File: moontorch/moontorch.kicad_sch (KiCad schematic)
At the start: 27 parts, among them J1 Conn_Coaxial, J2 Pogo_VLED_1, J3 Pogo_VLED_2, J4 BAT, J5 Torchbutton, J6 UART, J7 USB, J8 Pogo_GND, Q1 AP2317SD, SW3 RESET, SW4 BOOT, U1 HT-CT62, U2 L80-R, U3 XTX XTP2038-330AS2CT

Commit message: weiter moontorch
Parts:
- removed J1: Conn_Coaxial, Connector_Coaxial:SMA_Amphenol_132289_EdgeMount, symbol Connector:Conn_Coaxial
- added C8: 1u, Capacitor_SMD:C_0603_1608Metric_Pad1.08x0.95mm_HandSolder, symbol Device:C
- added R6: 0R, Resistor_SMD:R_0603_1608Metric_Pad0.98x0.95mm_HandSolder, symbol Device:R
- added R8, R9: 10K, Resistor_SMD:R_0603_1608Metric_Pad0.98x0.95mm_HandSolder, symbol Device:R
- added RF1: 443MHz, EasyEDA:SMA-SMD_BWSMA-KE-P001, symbol EasyEDA:HJ-SMA275
- added U4: 2.4GHz, EasyEDA:ANT-SMD_L5.0-W2.0, symbol EasyEDA:2450AT42A100E
- C1, C2, C7: LCSC Part (none) -> C15849
- C3, C4: LCSC Part (none) -> C14663
- C5, C6: LCSC Part (none) -> C19702
- J2, J3, J8: footprint TestPoint:TestPoint_Pad_3.0x3.0mm -> hacrafu:Pogo Pin 3015; LCSC Part (none) -> C5221293
- J4: footprint Connector_JST:JST_XH_B2B-XH-A_1x02_P2.50mm_Vertical -> Connector_PinHeader_2.54mm:PinHeader_1x02_P2.54mm_Horizontal
- R1, R2, R3: LCSC Part (none) -> C98220
- R4, R5: LCSC Part (none) -> C25803
- U3: LCSC Part (none) -> C7422361
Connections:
- net +3V3: now also C8.1, R8.2, R9.1
- net GND: now also C8.2, RF1.1, RF1.2, RF1.3, RF1.4
- net GPS_PPS: now also R9.2
- net USB_DN: now reaches U1.17 (GPIO18_DN)
- net USB_DN: now also J7.3 (Pin_3); no longer J7.2 (Pin_2)
- net USB_DP: now reaches U1.18 (GPIO19_DP)
- net USB_DP: now also J7.2 (Pin_2); no longer J7.3 (Pin_3)
- net at U1.22 (LoRa_Ant): now also RF1.5
- net UART_TX: now reaches J6.2 (Pin_2), U1.20 (GPIO21_TXD)
- net UART_RX: now reaches J6.3 (Pin_3), U1.19 (GPIO20_RXD)
- net at U1.1 (2.4G_Ant): now also R6.2
- net at U1.16 (GPIO8): now also R8.1
- new net: R6.1, U4.1 (ANT)
- no-connect marks 4 -> 6
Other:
- moved on the sheet: C7, J5, J7

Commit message: zwischenstand bestellfähig 1
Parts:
- removed BT1: Battery, hacrafu:Battery 230525, symbol Device:Battery
- removed J2: Pogo_VLED_1, hacrafu:Pogo Pin 3015, symbol Connector:Conn_01x01_Pin
- removed J3: Pogo_VLED_2, hacrafu:Pogo Pin 3015, symbol Connector:Conn_01x01_Pin
- removed J5: Torchbutton, hacrafu:Tochbutton GND, symbol Connector:Conn_01x01_Pin
- removed J7: USB, Connector_PinHeader_2.54mm:PinHeader_1x03_P2.54mm_Vertical, symbol Connector:Conn_01x03_Pin
- removed J8: Pogo_GND, hacrafu:Pogo Pin 3015, symbol Connector:Conn_01x01_Pin
- removed R6: 0R, Resistor_SMD:R_0603_1608Metric_Pad0.98x0.95mm_HandSolder, symbol Device:R
- removed RF1: 443MHz, EasyEDA:SMA-SMD_BWSMA-KE-P001, symbol EasyEDA:HJ-SMA275
- removed U4: 2.4GHz, EasyEDA:ANT-SMD_L5.0-W2.0, symbol EasyEDA:2450AT42A100E
- added C10, C12, C13, C9: 1u, Capacitor_SMD:C_0603_1608Metric_Pad1.08x0.95mm_HandSolder, symbol Device:C
- added C4, C7: 10u, Capacitor_SMD:C_0603_1608Metric_Pad1.08x0.95mm_HandSolder, symbol Device:C
- added D1, D2, D3: Schtky, EasyEDA:SOD-323_L1.8-W1.3-LS2.5-RD, symbol EasyEDA:1N5819WS
- added J3: LED, Connector_PinHeader_2.54mm:PinHeader_1x04_P2.54mm_Vertical, symbol Connector:Conn_01x04_Pin
- added JP1: SolderJumper_3_Open, Jumper:SolderJumper-3_P1.3mm_Open_Pad1.0x1.5mm, symbol Jumper:SolderJumper_3_Open
- added L1, L2: 10u, EasyEDA:IND-SMD_L5.4-W5.2_FXL0530, symbol EasyEDA:FXL0530-100-M
- added LED1: CHRG, LED_SMD:LED_0805_2012Metric_Pad1.15x1.40mm_HandSolder, symbol EasyEDA:17-21SUYC_TR8
- added Q1: AO3401A, EasyEDA:SOT-23_L2.9-W1.3-P1.90-LS2.4-BR, symbol EasyEDA:AO3401A
- added R1, R2: 5k1, Resistor_SMD:R_0603_1608Metric_Pad0.98x0.95mm_HandSolder, symbol EasyEDA:0603WAF5101T5E
- added R11: 1k, Resistor_SMD:R_0603_1608Metric_Pad0.98x0.95mm_HandSolder, symbol EasyEDA:0603WAF1001T5E
- added R14, R15: 0R5, Resistor_SMD:R_1206_3216Metric_Pad1.30x1.75mm_HandSolder, symbol EasyEDA:1206W4F500LT5E
- added R4: 10K, Resistor_SMD:R_0603_1608Metric_Pad0.98x0.95mm_HandSolder, symbol Device:R
- added R5: 330, Resistor_SMD:R_0603_1608Metric_Pad0.98x0.95mm_HandSolder, symbol EasyEDA:0603WAF3300T5E
- added R7: 1k5, Resistor_SMD:R_0603_1608Metric_Pad0.98x0.95mm_HandSolder, symbol EasyEDA:0603WAF1501T5E
- added SW1: BTN, EasyEDA:SW-SMD_6P-L5.8-W5.8-P2.00-LS8.5-TR, symbol EasyEDA:XKB5858-Z-TP_C840833
- added SW4: ON OFF, EasyEDA:SW-TH_K3-1296S-E1, symbol EasyEDA:K3-1296S-E1_C128955
- added U2: TP4056, EasyEDA:ESOP-8_L4.9-W3.9-P1.27-LS6.0-BL-EP, symbol EasyEDA:TP4056
- added U4, U5: MT9201, EasyEDA:SOT-23-6_L2.9-W1.6-P0.95-LS2.8-BR, symbol EasyEDA:MT9201
- added USB1: USB-TYPE-C-018, EasyEDA:USB-C_SMD-TYPE-C-31-M-12, symbol EasyEDA:USB-TYPE-C-018
- J1: renamed from J4; footprint Connector_PinHeader_2.54mm:PinHeader_1x02_P2.54mm_Horizontal -> hacrafu:Battery 230525; symbol Connector:Conn_01x02_Pin -> Device:Battery
- U6: renamed from U3; value XTX XTP2038-330AS2CT -> LDO 3V3
- renumbered C5 to C1, C1 to C11, C2 to C14, C4 to C2, C7 to C3, C8 to C5, C3 to C8, J6 to J2, Q1 to Q2, R5 to R10, R1 to R12, R2 to R13, R9 to R6, R4 to R9, SW4 to SW2, U2 to U1, U1 to U3
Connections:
- net GND: now also C10.2, C12.2, C13.2, C4.2, C7.2, C9.2, JP1.1 (A), R1.1, R14.1, R15.1, R2.2, R4.2, R7.1, U2.1 (TEMP), U2.3 (GND), U2.9 (EP), U4.2 (GND), U5.2 (GND), USB1.0 (SH), USB1.1 (SH), USB1.2 (SH), USB1.3 (SH), USB1.A1 (GND), USB1.A12 (GND), USB1.B1 (GND), USB1.B12 (GND); no longer U6.3 (ON/~{OFF})
- net LED1: now also U4.4 (EN)
- net LED2: now also U5.4 (EN)
- net USB_DN: now also USB1.A7 (DN1), USB1.B7 (DN2)
- net USB_DP: now also USB1.A6 (DP1), USB1.B6 (DP2)
- net VBAT: now also C7.1, Q1.3 (D), SW4.3, U2.5 (BAT); no longer C11.1, J1.1 (Pin_1), Q2.1 (S1), Q2.3 (S2), R12.1, R13.1, U6.1 (VIN)
- net at C3.1: now also SW1.1; no longer U3.9 (GPIO1)
- net VLED1 renamed LED1_A
- net LED1_A: now also C12.1, D2.1 (K), J3.4 (Pin_4), U4.5 (OV)
- net VLED2 renamed LED2_A
- net LED2_A: now also C13.1, D3.1 (K), J3.1 (Pin_1), U5.5 (OV)
- new net: D2.2 (A), L1.2, U4.1 (SW)
- new net: R7.2, U2.2 (PROG)
- new net: R5.2, U2.7 (~{CHRG})
- new net: LED1.2 (-), R5.1
- new net: D3.2 (A), L2.2, U5.1 (SW)
- new net: R2.1, USB1.A5 (CC1)
- new net: R1.2, USB1.B5 (CC2)
- new net: Q1.1 (G), R11.1
- new net: JP1.2 (C), U6.3 (ON/~{OFF})
- new net 5V: C4.1, D1.2 (A), LED1.1 (+), R11.2, R4.1, U2.4 (VCC), U2.8 (CE), USB1.A4 (VBUS), USB1.A9 (VBUS), USB1.B4 (VBUS), USB1.B9 (VBUS)
- new net BTN: SW1.2, U3.9 (GPIO1)
- new net LED1_C: J3.3 (Pin_3), R14.2, U4.3 (FB)
- new net LED2_C: J3.2 (Pin_2), R15.2, U5.3 (FB)
- new net VBAT_PRE: J1.1 (+), SW4.2
- new net VBUS: C10.1, C11.1, C9.1, D1.1 (K), JP1.3 (B), L1.1, L2.1, Q1.2 (S), Q2.1 (S1), Q2.3 (S2), R12.1, R13.1, U4.6 (VIN), U5.6 (VIN), U6.1 (VIN)
- no-connect marks 6 -> 19
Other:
- moved on the sheet: C11, C14, C3, C8, Q2, R10, R12, R13, R3, R8, R9, SW2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

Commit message: bestellung
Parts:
- removed C14: 1u, Capacitor_SMD:C_0603_1608Metric_Pad1.08x0.95mm_HandSolder, symbol Device:C
- removed D2, D3: Schtky, EasyEDA:SOD-323_L1.8-W1.3-LS2.5-RD, symbol EasyEDA:1N5819WS
- removed JP1: SolderJumper_3_Open, Jumper:SolderJumper-3_P1.3mm_Open_Pad1.0x1.5mm, symbol Jumper:SolderJumper_3_Open
- removed L1, L2: 10u, EasyEDA:IND-SMD_L5.4-W5.2_FXL0530, symbol EasyEDA:FXL0530-100-M
- removed R7: 1k5, Resistor_SMD:R_0603_1608Metric_Pad0.98x0.95mm_HandSolder, symbol EasyEDA:0603WAF1501T5E
- removed U4, U5: MT9201, EasyEDA:SOT-23-6_L2.9-W1.6-P0.95-LS2.8-BR, symbol EasyEDA:MT9201
- removed U6: LDO 3V3, Package_TO_SOT_SMD:SOT-23-5_HandSoldering, symbol Regulator_Linear:LP2985-3.3
- added J4, J5, J6: BAT1, Connector_PinHeader_2.54mm:PinHeader_1x02_P2.54mm_Vertical, symbol Connector:Conn_01x02_Pin
- added R16: 100K, Resistor_SMD:R_0603_1608Metric_Pad0.98x0.95mm_HandSolder, symbol Device:R
- added R7: 1k2, Resistor_SMD:R_0603_1608Metric_Pad0.98x0.95mm_HandSolder, symbol EasyEDA:0603WAF1201T5E
- added U4: RT9080-33GJ5, EasyEDA:TSOT-23-5_L2.9-W1.6-P0.95-LS2.8-BL, symbol EasyEDA:RT9080-33GJ5
- C12, C13: value 1u -> C; LCSC Part C15849 -> (none); now not fitted; now left out of the parts list
- C9: value 1u -> 10u; LCSC Part C15849 -> C19702
- J2, J3: now left out of the parts list
- R12, R13, R3, R4, R6, R8: LCSC Part C98220 -> C25804
- U1: footprint RF_GPS:Quectel_L80-R -> hacrafu:Quectel_L80-R; now left out of the parts list
- U3: footprint RF_Module:Heltec_HT-CT62 -> hacrafu:Heltec_HT-CT62; now left out of the parts list
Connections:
- net +3V3: now also C1.1, C2.1, C9.1, U1.4 (VCC), U4.5 (VOUT)
- net GND: now also C12.1, J4.1 (Pin_1), J5.1 (Pin_1), J6.1 (Pin_1), R7.1, U4.2 (GND); no longer C12.2
- net LED1_A: now also C12.2, J3.1 (Pin_1); no longer C12.1, J3.4 (Pin_4)
- net LED2_A: now also J3.2 (Pin_2); no longer J3.1 (Pin_1)
- net LED2_C: now also J3.4 (Pin_4); no longer J3.2 (Pin_2)
- net VBAT: now also Q2.1 (S1), Q2.3 (S2), R12.1, R13.1; no longer C1.1, C2.1, R9.1, U1.4 (VCC)
- net VBAT_PRE: now also R9.1, J4.2 (Pin_2), J5.2 (Pin_2), J6.2 (Pin_2)
- net VBUS: now also R16.1, U4.1 (VIN); no longer C9.1, Q2.1 (S1), Q2.3 (S2), R12.1, R13.1
- net at U2.2 (PROG): now also R7.2
- new net: R16.2, U4.3 (EN)
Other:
- moved on the sheet: C8, J1, J3, Q2, R10, R12, R13, R14, R15, R9, SW4

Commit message: pcb dnp
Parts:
- J2, J3: now not fitted
- J4, J5, J6: now not fitted; now left out of the parts list
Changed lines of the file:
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@@
 		(unit 1)
 		(exclude_from_sim no)
-		(in_bom yes)
+		(in_bom no)
 		(on_board yes)
-		(dnp no)
+		(dnp yes)
 		(property "Reference" "J6"
 			(at 274.955 81.28 0)
@@
 		(in_bom no)
 		(on_board yes)
-		(dnp no)
+		(dnp yes)
 		(property "Reference" "J3"
 			(at 275.59 33.0201 0)
@@
 		(unit 1)
 		(exclude_from_sim no)
-		(in_bom yes)
+		(in_bom no)
 		(on_board yes)
-		(dnp no)
+		(dnp yes)
 		(property "Reference" "J5"
 			(at 258.445 81.28 0)
@@
 		(in_bom no)
 		(on_board yes)
-		(dnp no)
+		(dnp yes)
 		(fields_autoplaced yes)
 		(property "Reference" "J2"
@@
 		(unit 1)
 		(exclude_from_sim no)
-		(in_bom yes)
+		(in_bom no)
 		(on_board yes)
-		(dnp no)
+		(dnp yes)
 		(property "Reference" "J4"
 			(at 243.205 81.28 0)

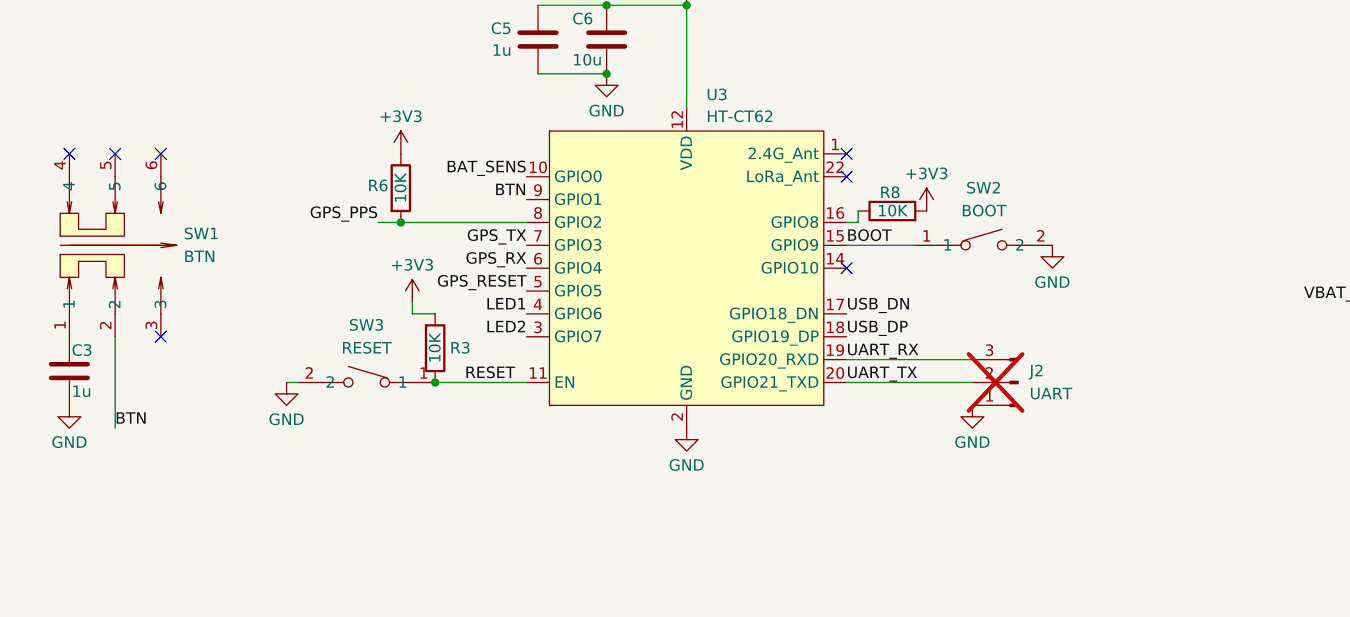
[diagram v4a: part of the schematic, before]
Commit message: moontorch schematic pin labels
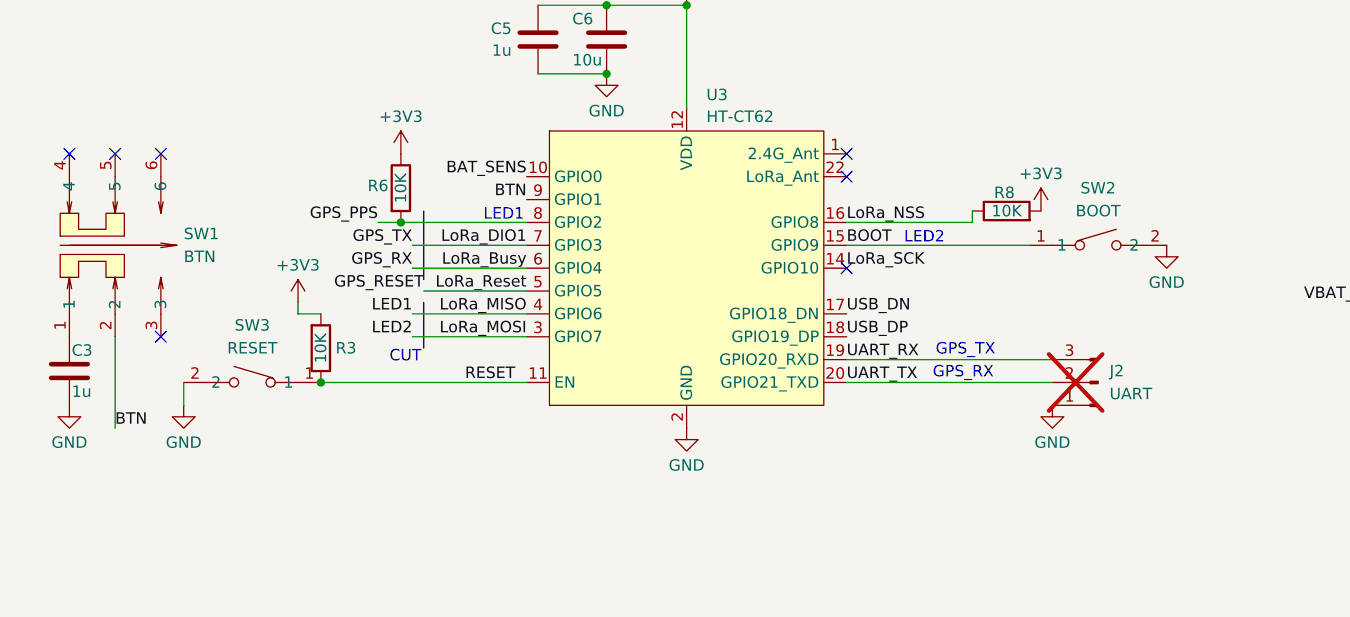
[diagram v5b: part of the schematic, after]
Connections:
- net LoRa_NSS: now reaches R8.1, U3.16 (GPIO8)
- net LoRa_SCK: now reaches U3.14 (GPIO10)
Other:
- note added: "CUT"
- note added: "GPS_RX"
- note added: "GPS_TX"
- note added: "LED1"
- note added: "LED2"
- moved on the sheet: J2, R3, R8, SW2, SW3
